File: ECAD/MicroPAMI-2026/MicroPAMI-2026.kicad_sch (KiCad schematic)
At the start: 37 parts, among them J1 Conn_01x05, J13 OLED, J2 Conn_01x05, J3 MicroServo 2G, J5 UPDI, SW2 Left, SW3 Right, SW4 SW_SPDT, SW5 SW_DIP_x01, U1 ATtiny3226-S, U2 ITR9608-F, U4 AMS1117-5.0, U5 ULN2803A

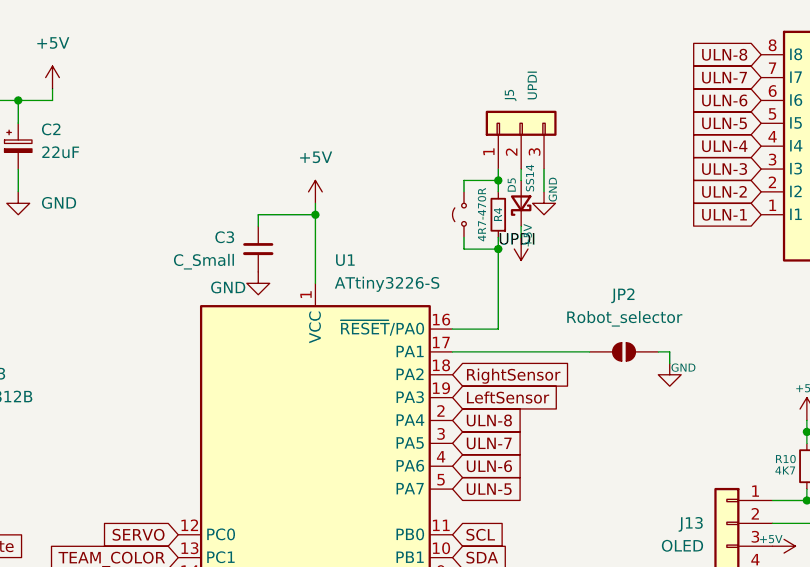
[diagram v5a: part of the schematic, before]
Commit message: change uC value
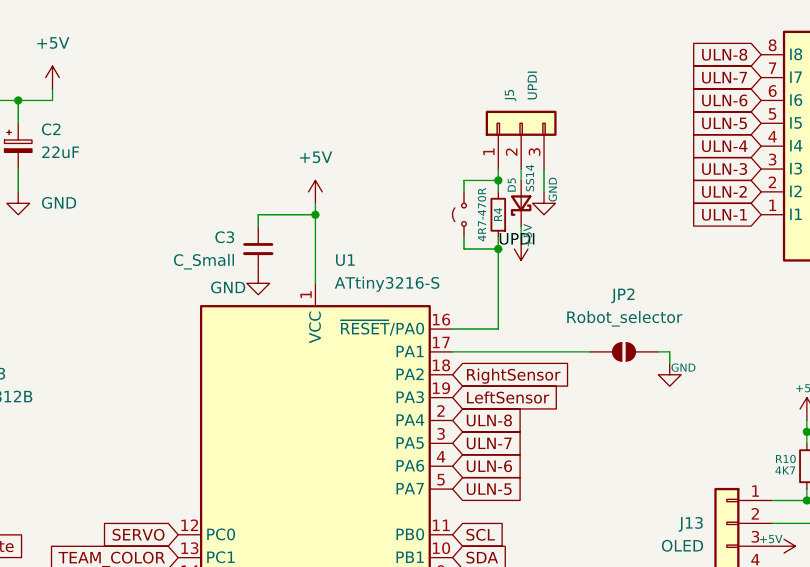
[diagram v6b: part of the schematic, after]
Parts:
- U1: value ATtiny3226-S -> ATtiny3216-S
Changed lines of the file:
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@@
 			)
 		)
-		(property "Value" "ATtiny3226-S"
+		(property "Value" "ATtiny3216-S"
 			(at 97.3933 45.72 0)
 			(effects
